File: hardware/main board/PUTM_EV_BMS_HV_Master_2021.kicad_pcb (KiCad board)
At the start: 4 copper layers, 60 x 150 mm, 250 parts, among them IC1 MCP1501-10E_SN, IC10 REF193GSZ-REEL, IC11 AP7365-33YRG-13, IC12 UCC12040DVE, IC13 MAX17643ATC+, IC14 RTQ2965GSP-QA, IC15 ISO6763FDWR, IC16 ISO6763FDWR, IC17 UCC12040DVE, IC2 MCP3561T-E_NC, IC3 REF193GSZ-REEL, IC4 MCP3561T-E_NC, IC6 AP7365-33YRG-13, IC7 MCP3562T-E_NC, IC9 REF193GSZ-REEL, J1 USB4145-03-0070-C, J10 M80-5100622, J11 M80-5101422, J14 Conn_01x05, J16 TagConnect, J2 M80-5103422, J4 M300-MV10345M1, J5 M300-MV10345M1, J6 M80-5100442, J9 M300-MV30645M1, K2 6-1419128-4, Q1 2SK3065, Q10 Q_NMOS_GSD, Q11 Q_NMOS_GSD, Q12 2SK3065, Q13 2SK3065, Q14 2SK3065, Q15 2SK3065, Q2 2N7002, Q3 Q_NMOS_GDS, Q4 2N7002, Q5 Q_NMOS_GDS, Q6 Q_NMOS_GDS, Q7 2SK3065, Q8 Q_PMOS_GSD, Q9 2SK3065, T1 HX1188NL, U1 USBLC6-2SC6, U12 LTC6820IMS, U13 LTC6820IMS, U14 74AUP1G32, U2 STM32G484RETx, U3 MCP2542FDxMF, U4 USBLC6-2SC6, U5 LM1117-3.3, U6 MCP2542FDxMF, U8 74LVC1G86, Y1 20MHz, Y2 32.768kHz

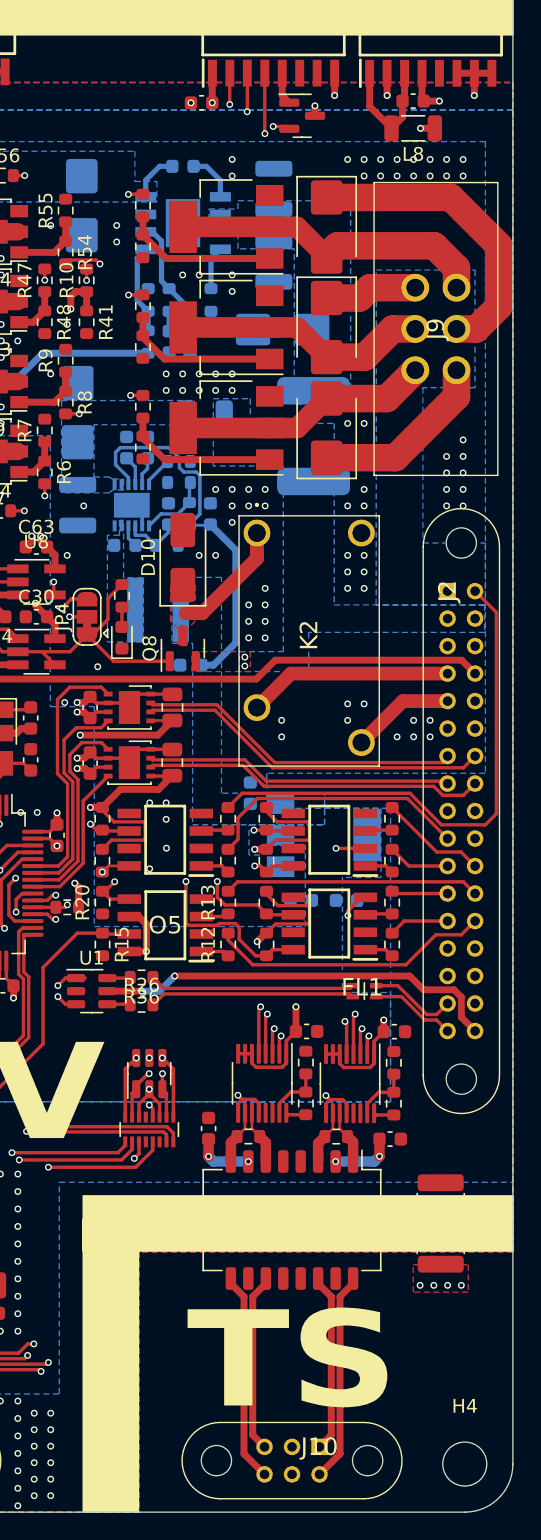
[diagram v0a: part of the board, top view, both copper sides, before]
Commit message: slight changes, changed shield's coupling resitor to a couplingcapacitor
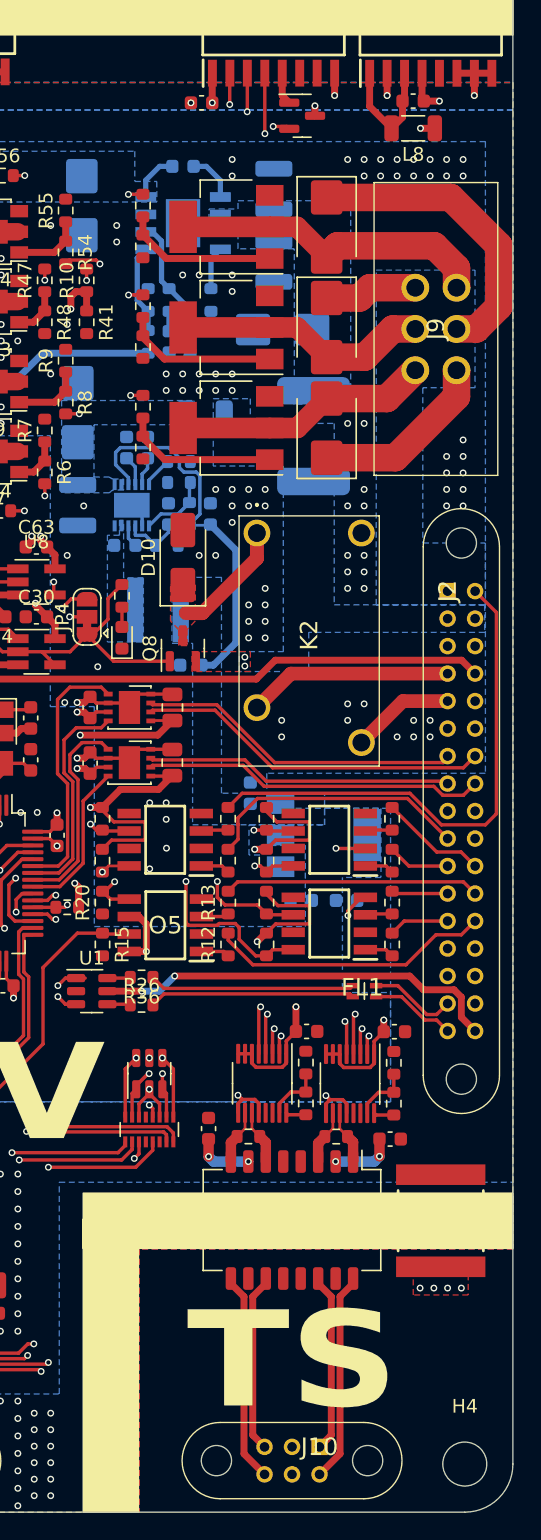
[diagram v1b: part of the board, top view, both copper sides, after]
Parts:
- removed R25: 10M, Resistor_SMD:R_2512_6332Metric
- added C27: 5.6nF, Samacsys:C2824, F.Cu at (161.8, 161.8)
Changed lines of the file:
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@@
       (rotate (xyz 0 0 0))
     )
+    (model "${KIPRJMOD}/footprint/Samacsys.3dshapes/HX1188NLT.stp"
+      (offset (xyz 0 0 0))
+      (scale (xyz 1 1 1))
+      (rotate (xyz -90 0 90))
+    )
   )
   (footprint "Capacitor_SMD:C_0603_1608Metric" (layer "F.Cu")
@@
     )
   )
+  (footprint "Samacsys:C2824" (layer "F.Cu")
+    (at 161.75 161.8 -90)
+    (descr "C2824")
+    (tags "Capacitor")
+    (property "Description" "SMD Auto C0G HV, Ceramic, 5600 pF, 5%, 2000 VDC, 2400 VDC, 125C, -55C, C0G, SMD, MLCC, Ultra-Stable, Low Loss, High Voltage, Automotive Grade, 0.1 % , 100 GOhms, 540 mg, 2824, 7.1mm, 6.1mm, 2.5mm, 1.27mm, 300, 78  Weeks, 120")
+    (property "Height" "")
+    (property "Manufacturer_Name" "KEMET")
+    (property "Manufacturer_Part_Number" "C2824C562JGGACAUTO")
+    (property "Mouser Part Number" "80-C2824C562JGGAUTO")
+    (property "Mouser Price/Stock" "https://www.mouser.co.uk/ProductDetail/KEMET/C2824C562JGGACAUTO?qs=5aG0NVq1C4xKMWO6DzsxHA%3D%3D")
+    (property "Sheetfile" "Connectors.kicad_sch")
+    (property "Sheetname" "Connectors")
+    (property "ki_description" "SMD Auto C0G HV, Ceramic, 5600 pF, 5%, 2000 VDC, 2400 VDC, 125C, -55C, C0G, SMD, MLCC, Ultra-Stable, Low Loss, High Voltage, Automotive Grade, 0.1 % , 100 GOhms, 540 mg, 2824, 7.1mm, 6.1mm, 2.5mm, 1.27mm, 300, 78  Weeks, 120")
+    (attr smd)
+    (fp_text reference "C27" (at 0 0 90) (layer "F.SilkS")
+        (effects (font (size 1.27 1.27) (thickness 0.254)))
+    )
+    (fp_text value "5.6nF" (at 0 0 90) (layer "F.SilkS") hide
+        (effects (font (size 1.27 1.27) (thickness 0.254)))
+    )
+    (fp_text user "${REFERENCE}" (at 0 0 90) (layer "F.Fab")
+        (effects (font (size 1.27 1.27) (thickness 0.254)))
+    )
+    (fp_line (start -2.2 -3.1) (end 2.2 -3.1)
+      (stroke (width 0.2) (type solid)) (layer "F.SilkS"))
+    (fp_line (start -2.2 3.1) (end 2.2 3.1)
+      (stroke (width 0.2) (type solid)) (layer "F.SilkS"))
+    (fp_line (start -4.9 -4.05) (end 4.9 -4.05)
+      (stroke (width 0.05) (type solid)) (layer "F.CrtYd"))
+    (fp_line (start -4.9 4.05) (end -4.9 -4.05)
+      (stroke (width 0.05) (type solid)) (layer "F.CrtYd"))
+    (fp_line (start 4.9 -4.05) (end 4.9 4.05)
+      (stroke (width 0.05) (type solid)) (layer "F.CrtYd"))
+    (fp_line (start 4.9 4.05) (end -4.9 4.05)
+      (stroke (width 0.05) (type solid)) (layer "F.CrtYd"))
+    (fp_line (start -3.55 -3.05) (end 3.55 -3.05)
+      (stroke (width 0.2) (type solid)) (layer "F.Fab"))
+    (fp_line (start -3.55 3.05) (end -3.55 -3.05)
+      (stroke (width 0.2) (type solid)) (layer "F.Fab"))
+    (fp_line (start 3.55 -3.05) (end 3.55 3.05)
+      (stroke (width 0.2) (type solid)) (layer "F.Fab"))
+    (fp_line (start 3.55 3.05) (end -3.55 3.05)
+      (stroke (width 0.2) (type solid)) (layer "F.Fab"))
+    (pad "1" smd rect (at -3.35 0 270) (size 1.5 6.5) (layers "F.Cu" "F.Paste" "F.Mask")
+      (net 1 "GND") (pintype "passive") (zone_connect 1) (thermal_bridge_width 2) (thermal_gap 0.2))
+    (pad "2" smd rect (at 3.35 0 270) (size 1.5 6.5) (layers "F.Cu" "F.Paste" "F.Mask")
+      (net 152 "/Connectors/LTC_CHASSIS") (pintype "passive"))
+    (model "${KIPRJMOD}/footprint/Samacsys.3dshapes/C2824C562JGGACAUTO.stp"
+      (offset (xyz 99.5 41 -11))
+      (scale (xyz 1 1 1))
+      (rotate (xyz -90 0 0))
+    )
+  )
   (footprint "Resistor_SMD:R_0603_1608Metric" (layer "F.Cu")
     (at 135.992 96.441 -90)
@@
     )
   )
-  (footprint "Resistor_SMD:R_2512_6332Metric" (layer "F.Cu")
-    (at 161.75 162 -90)
-    (descr "Resistor SMD 2512 (6332 Metric), square (rectangular) end terminal, IPC_7351 nominal, (Body size source: IPC-SM-782 page 72, https://www.pcb-3d.com/wordpress/wp-content/uploads/ipc-sm-782a_amendment_1_and_2.pdf), generated with kicad-footprint-generator")
-    (tags "resistor")
-    (property "Sheetfile" "Connectors.kicad_sch")
-    (property "Sheetname" "Connectors")
-    (property "ki_description" "Resistor, small symbol")
-    (property "ki_keywords" "R resistor")
-    (attr smd)
-    (fp_text reference "R25" (at 0 -2.62 90) (layer "F.SilkS")
-        (effects (font (size 1 1) (thickness 0.15)))
-    )
-    (fp_text value "10M" (at 0 2.62 90) (layer "F.Fab")
-        (effects (font (size 1 1) (thickness 0.15)))
-    )
-    (fp_text user "${REFERENCE}" (at 0 0 90) (layer "F.Fab")
-        (effects (font (size 1 1) (thickness 0.15)))
-    )
-    (fp_line (start -2.177064 -1.71) (end 2.177064 -1.71)
-      (stroke (width 0.12) (type solid)) (layer "F.SilkS"))
-    (fp_line (start -2.177064 1.71) (end 2.177064 1.71)
-      (stroke (width 0.12) (type solid)) (layer "F.SilkS"))
-    (fp_line (start -3.82 -1.92) (end 3.82 -1.92)
-      (stroke (width 0.05) (type solid)) (layer "F.CrtYd"))
-    (fp_line (start -3.82 1.92) (end -3.82 -1.92)
-      (stroke (width 0.05) (type solid)) (layer "F.CrtYd"))
-    (fp_line (start 3.82 -1.92) (end 3.82 1.92)
-      (stroke (width 0.05) (type solid)) (layer "F.CrtYd"))
-    (fp_line (start 3.82 1.92) (end -3.82 1.92)
-      (stroke (width 0.05) (type solid)) (layer "F.CrtYd"))
-    (fp_line (start -3.15 -1.6) (end 3.15 -1.6)
-      (stroke (width 0.1) (type solid)) (layer "F.Fab"))
-    (fp_line (start -3.15 1.6) (end -3.15 -1.6)
-      (stroke (width 0.1) (type solid)) (layer "F.Fab"))
-    (fp_line (start 3.15 -1.6) (end 3.15 1.6)
-      (stroke (width 0.1) (type solid)) (layer "F.Fab"))
-    (fp_line (start 3.15 1.6) (end -3.15 1.6)
-      (stroke (width 0.1) (type solid)) (layer "F.Fab"))
-    (pad "1" smd roundrect (at -2.9625 0 270) (size 1.225 3.35) (layers "F.Cu" "F.Paste" "F.Mask") (roundrect_rratio 0.204082)
-      (net 1 "GND") (pintype "passive") (zone_connect 1) (thermal_bridge_width 3) (thermal_gap 0.2))
-    (pad "2" smd roundrect (at 2.9625 0 270) (size 1.225 3.35) (layers "F.Cu" "F.Paste" "F.Mask") (roundrect_rratio 0.204082)
-      (net 152 "/Connectors/LTC_CHASSIS") (pintype "passive"))
-    (model "${KICAD6_3DMODEL_DIR}/Resistor_SMD.3dshapes/R_2512_6332Metric.wrl"
-      (offset (xyz 0 0 0))
-      (scale (xyz 1 1 1))
-      (rotate (xyz 0 0 0))
-    )
-  )
   (footprint "Capacitor_SMD:C_0603_1608Metric" (layer "F.Cu")
     (at 129.9 144.71 180)
@@
   (gr_rect (start 107 71.5) (end 167 75.5254)
     (stroke (width 0.12) (type solid)) (fill solid) (layer "B.SilkS"))
-  (gr_rect (start 135.75 160) (end 167 164)
+  (gr_rect (start 135.775 159.8) (end 167.025 163.8)
     (stroke (width 0.12) (type solid)) (fill solid) (layer "B.SilkS"))
   (gr_rect (start 135.75 161.7119) (end 139.74 182.9873)
@@
   (gr_rect (start 107 71.5) (end 167 75.5254)
     (stroke (width 0.12) (type solid)) (fill solid) (layer "F.SilkS"))
-  (gr_rect (start 135.75 160) (end 167 164)
+  (gr_rect (start 135.75 159.8) (end 167 163.8)
     (stroke (width 0.12) (type solid)) (fill solid) (layer "F.SilkS"))
   (gr_line (start 167 179.5) (end 167 36.5)
@@
   (segment (start 159.293 149.377) (end 164.853 149.377) (width 0.25) (layer "In2.Cu") (net 151))
   (segment (start 146.11 151.025) (end 157.645 151.025) (width 0.25) (layer "In2.Cu") (net 151))
-  (via (at 163.25 166.5) (size 0.5) (drill 0.3) (layers "F.Cu" "B.Cu") (free) (net 152))
-  (via (at 160.25 166.5) (size 0.5) (drill 0.3) (layers "F.Cu" "B.Cu") (free) (net 152))
-  (via (at 162.25 166.5) (size 0.5) (drill 0.3) (layers "F.Cu" "B.Cu") (free) (net 152))
-  (via (at 161.25 166.5) (size 0.5) (drill 0.3) (layers "F.Cu" "B.Cu") (free) (net 152))
+  (via (at 163.25 166.7) (size 0.5) (drill 0.3) (layers "F.Cu" "B.Cu") (free) (net 152))
+  (via (at 160.25 166.7) (size 0.5) (drill 0.3) (layers "F.Cu" "B.Cu") (free) (net 152))
+  (via (at 162.25 166.7) (size 0.5) (drill 0.3) (layers "F.Cu" "B.Cu") (free) (net 152))
+  (via (at 161.25 166.7) (size 0.5) (drill 0.3) (layers "F.Cu" "B.Cu") (free) (net 152))
   (segment (start 152.835 166.005) (end 152.835 166.367516) (width 0.508) (layer "F.Cu") (net 153))
   (segment (start 153.79 177.394) (end 152.934 178.25) (width 0.508) (layer "F.Cu") (net 153))
@@
         (xy 159.75 165)
         (xy 163.75 165)
-        (xy 163.75 167)
-        (xy 159.75 167)
+        (xy 163.75 167.2)
+        (xy 159.75 167.2)
       )
     )
@@
         (xy 107 79)
         (xy 167 79)
-        (xy 167 164.07)
-        (xy 139.82 164.07)
+        (xy 167 163.87)
+        (xy 139.82 163.87)
         (xy 139.82 183)
         (xy 107 183)
@@
     (polygon
       (pts
-        (xy 163.55 158.2)
-        (xy 163.55 158.6)
-        (xy 159.95 158.6)
-        (xy 159.95 158.2)
         (xy 134 158.2)
         (xy 134 183)
         (xy 139.825 183)
-        (xy 139.825 164.075)
-        (xy 167 164.075)
+        (xy 139.825 163.875)
+        (xy 167 163.875)
         (xy 167 158.2)
       )
@@
     (members
       1953f8b9-efd0-4443-8520-6916507a8a53
-      d688ac50-b347-4941-9c4c-9c17cd3f6923
       db9c3a50-41be-4189-8a3e-3e2182aa3410
       f86030ca-cdb6-42e2-9341-1f0357125150
@@
   (group "" (id a1fba123-85ce-4549-bbf7-7d1244ff9987)
     (members
-      3714c240-f0ac-450e-bf30-ba2e34d971b7
       3859f0de-ce5a-446b-a0f8-a4791e950552
       3f78fdd8-0c6d-416b-9edd-8a0c4149e873
@@
     (members
       00683df5-0eb7-44dc-bc52-77dd65412676
-      008f9162-5796-4fef-90f6-e270dcff64e0
       0113a355-91cd-467a-b3f3-381ac5636d9a
       02b3d86e-dc48-4885-be79-453a05f02b94
@@
       90c40293-5396-4918-b144-7eb45af9d298
       93a19a66-3a76-4ed2-8285-e5d68ab34d27
-      98a4944c-6fb1-470f-b719-d637de73f9d5
       98f58df8-1d86-4d50-b52f-aba7334126e9
       9c7267bc-29b8-4d9d-8c49-e39f7360d9f6
@@
       ef4fb8cb-0824-4a92-881c-a034c8ba6970
       f12b8bcd-c5cf-4d80-84bc-c7da05631869
-      f2fcd06b-6a6e-4e62-8a33-66f1b89f049b
       f9beaf30-5b2b-436a-a865-6445c3cba42d
       f9d4080b-5d04-4287-b43d-adbffa15cdb5
@@
       c0705c50-0a32-4cb9-bc62-8a98554790c8
       cfcfc73a-e774-4144-bd71-4fbf23b680c7
-      d4086a7a-75b8-451c-8d8c-b401cdaadc3f
       d44c0dfd-ddab-408e-beb8-a0352ea71032
       dd755334-a385-44f4-8fdb-94bdaf6ca899
